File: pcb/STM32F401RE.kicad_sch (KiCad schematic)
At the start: 0 parts

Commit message: Connected oscillator to controller. Fixed local/hierarchical labeling in sheet.
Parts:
- added C5, C6: 22 pF, symbol Device:C
- added U3: STM32F401RETx, Package_QFP:LQFP-64_10x10mm_P0.5mm, symbol MCU_ST_STM32F4:STM32F401RETx
- added Y2: CX3225SB16000H0FLJCC, CX3225SB16000H0FLJCC:OSCCC320X250X60N, symbol 16 MHz Oscillator:CX3225SB16000H0FLJCC
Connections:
- new net: U3.18 (VSS), U3.31 (VSS), U3.47 (VSS), U3.63 (VSS)
- new net GND: Y2.2 (GND), Y2.4 (GND)

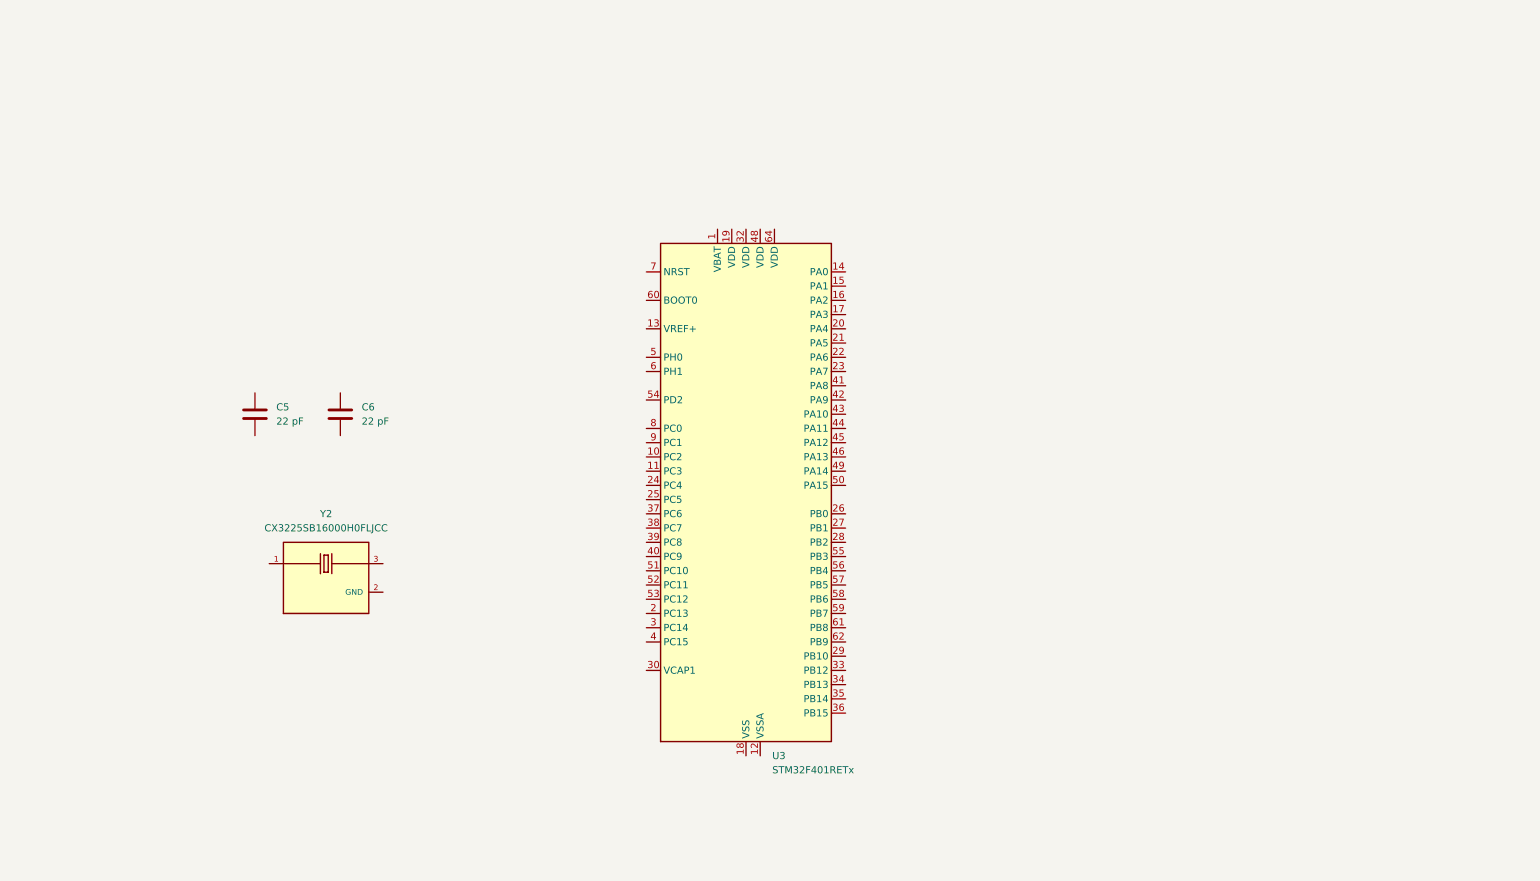
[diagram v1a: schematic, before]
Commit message: Added Front and Rear zone sheets made of CAN and MCU design sheets.
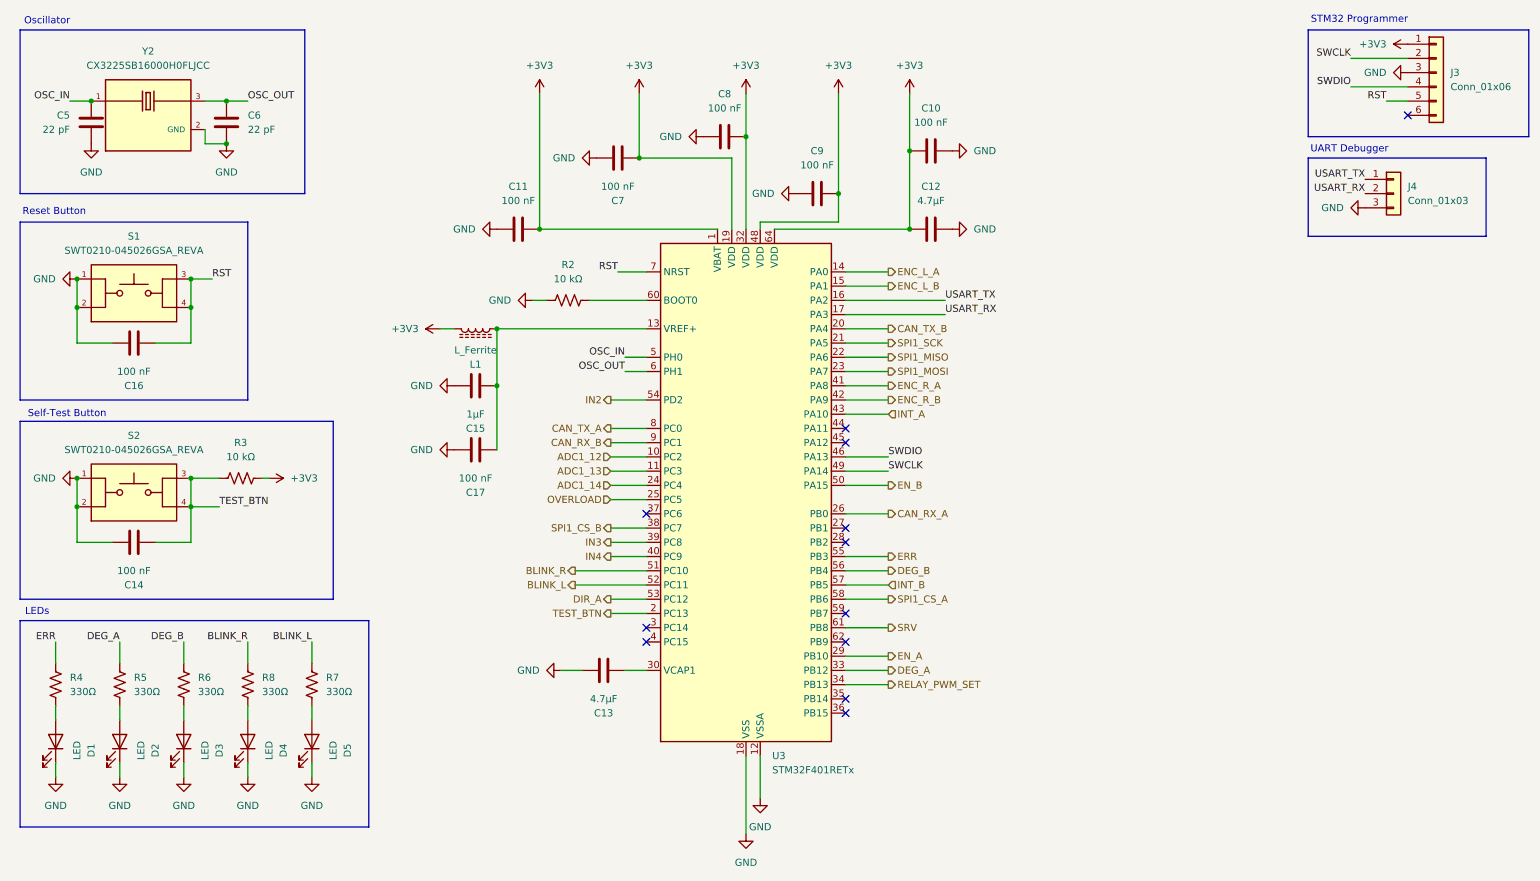
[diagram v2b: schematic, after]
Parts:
- added C10, C11, C14, C16, C17, C7, C8, C9: 100 nF, symbol Device:C
- added C12, C13: 4.7μF, symbol Device:C
- added C15: 1μF, symbol Device:C
- added D1, D2, D3, D4, D5: LED, symbol Device:LED
- added J3: Conn_01x06, symbol Connector_Generic:Conn_01x06
- added J4: Conn_01x03, symbol Connector_Generic:Conn_01x03
- added L1: L_Ferrite, symbol Device:L_Ferrite
- added R2, R3: 10 kΩ, symbol Device:R_US
- added R4, R5, R6, R7, R8: 330Ω, symbol Device:R_US
- added S1, S2: SWT0210-045026GSA_REVA, SWT0210-045026GSA_REVA:SW_SWT0210-045026GSA_REVA, symbol Push Button:SWT0210-045026GSA_REVA
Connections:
- net GND: now also C5.2, C6.2, U3.12 (VSSA), U3.18 (VSS), U3.31 (VSS), U3.47 (VSS), U3.63 (VSS), C10.1, C11.1, C12.2, C13.1, C14.1, C15.2, C16.1, C17.1, C7.1, C8.2, C9.1, D1.1 (K), D2.1 (K), D3.1 (K), D4.1 (K), D5.1 (K), J3.3 (Pin_3), J4.3 (Pin_3), R2.1, S1.1, S1.2, S2.1, S2.2
- net OSC_IN: now reaches C5.1
- net OSC_IN: now also U3.5 (PH0), Y2.1
- net +3V3: now reaches U3.1 (VBAT)
- net +3V3: now also U3.19 (VDD), U3.32 (VDD), U3.48 (VDD), U3.64 (VDD), C10.2, C11.2, C12.1, C7.2, C8.1, C9.2, J3.1 (Pin_1), L1.1, R3.2
- net ADC1_12: now reaches U3.10 (PC2)
- net ADC1_13: now reaches U3.11 (PC3)
- net at U3.13 (VREF+): now also C15.1, C17.2, L1.2
- net ENC_L_A: now reaches U3.14 (PA0)
- net ENC_L_B: now reaches U3.15 (PA1)
- net USART_TX: now reaches U3.16 (PA2)
- net USART_TX: now also J4.1 (Pin_1)
- net USART_RX: now reaches U3.17 (PA3)
- net USART_RX: now also J4.2 (Pin_2)
- net TEST_BTN: now reaches U3.2 (PC13)
- net TEST_BTN: now also C14.2, R3.1, S2.3, S2.4
- net CAN_TX_B: now reaches U3.20 (PA4)
- net SPI1_SCK: now reaches U3.21 (PA5)
- net SPI1_MISO: now reaches U3.22 (PA6)
- net SPI1_MOSI: now reaches U3.23 (PA7)
- net ADC1_14: now reaches U3.24 (PC4)
- net OVERLOAD: now reaches U3.25 (PC5)
- net CAN_RX_A: now reaches U3.26 (PB0)
- net EN_A: now reaches U3.29 (PB10)
- net at U3.30 (VCAP1): now also C13.2
- net DEG_A: now reaches U3.33 (PB12)
- net DEG_A: now also R5.1
- net RELAY_PWM_SET: now reaches U3.34 (PB13)
- net SPI1_CS_B: now reaches U3.38 (PC7)
- net IN3: now reaches U3.39 (PC8)
- net IN4: now reaches U3.40 (PC9)
- net ENC_R_A: now reaches U3.41 (PA8)
- net ENC_R_B: now reaches U3.42 (PA9)
- net INT_A: now reaches U3.43 (PA10)
- net SWDIO: now reaches U3.46 (PA13)
- net SWDIO: now also J3.4 (Pin_4)
- net SWCLK: now reaches U3.49 (PA14)
- net SWCLK: now also J3.2 (Pin_2)
- net EN_B: now reaches U3.50 (PA15)
- net BLINK_R: now reaches U3.51 (PC10)
- net BLINK_R: now also R8.1
- net BLINK_L: now reaches U3.52 (PC11)
- net BLINK_L: now also R7.1
- net DIR_A: now reaches U3.53 (PC12)
- net IN2: now reaches U3.54 (PD2)
- net ERR: now reaches U3.55 (PB3)
- net ERR: now also R4.1
- net DEG_B: now reaches U3.56 (PB4)
- net DEG_B: now also R6.1
- net INT_B: now reaches U3.57 (PB5)
- net SPI1_CS_A: now reaches U3.58 (PB6)
- net OSC_OUT: now reaches U3.6 (PH1)
- net OSC_OUT: now also C6.1, Y2.3
- net at U3.60 (BOOT0): now also R2.2
- net SRV: now reaches U3.61 (PB8)
- net RST: now reaches U3.7 (NRST)
- net RST: now also C16.2, J3.5 (Pin_5), S1.3, S1.4
- net CAN_TX_A: now reaches U3.8 (PC0)
- net CAN_RX_B: now reaches U3.9 (PC1)
- new net: D2.2 (A), R5.2
- new net: D4.2 (A), R8.2
- new net: D5.2 (A), R7.2
- new net: D1.2 (A), R4.2
- new net: D3.2 (A), R6.2
- no-connect marks 0 -> 12
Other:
- note added: "LEDs"
- note added: "Oscillator"
- note added: "Reset Button"
- note added: "STM32 Programmer"
- note added: "Self-Test Button"
- note added: "UART Debugger"
- moved on the sheet: C5, C6, Y2

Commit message: Added footprints to all components.
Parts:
- C701: renamed from C5; value 22 pF -> 22pF; footprint (none) -> Capacitor_SMD:C_0603_1608Metric
- C702: renamed from C16; value 100 nF -> 100nF; footprint (none) -> Capacitor_SMD:C_0603_1608Metric
- C703: renamed from C14; value 100 nF -> 100nF; footprint (none) -> Capacitor_SMD:C_0603_1608Metric
- C704: renamed from C6; value 22 pF -> 22pF; footprint (none) -> Capacitor_SMD:C_0603_1608Metric
- C705: renamed from C15; footprint (none) -> Capacitor_SMD:C_0603_1608Metric
- C706: renamed from C17; value 100 nF -> 100nF; footprint (none) -> Capacitor_SMD:C_0603_1608Metric
- C707: renamed from C11; value 100 nF -> 100nF; footprint (none) -> Capacitor_SMD:C_0603_1608Metric
- C708: renamed from C13; footprint (none) -> Capacitor_SMD:C_0805_2012Metric
- C709: renamed from C7; value 100 nF -> 100nF; footprint (none) -> Capacitor_SMD:C_0603_1608Metric
- C710: renamed from C8; value 100 nF -> 100nF; footprint (none) -> Capacitor_SMD:C_0603_1608Metric
- C711: renamed from C9; value 100 nF -> 100nF; footprint (none) -> Capacitor_SMD:C_0603_1608Metric
- C712: renamed from C10; value 100 nF -> 100nF; footprint (none) -> Capacitor_SMD:C_0603_1608Metric
- C713: renamed from C12; footprint (none) -> Capacitor_SMD:C_0805_2012Metric
- D701: renamed from D1; footprint (none) -> LED_SMD:LED_0603_1608Metric
- D702: renamed from D2; footprint (none) -> LED_SMD:LED_0603_1608Metric
- D703: renamed from D3; footprint (none) -> LED_SMD:LED_0603_1608Metric
- D704: renamed from D4; footprint (none) -> LED_SMD:LED_0603_1608Metric
- D705: renamed from D5; footprint (none) -> LED_SMD:LED_0603_1608Metric
- J701: renamed from J4; footprint (none) -> Connector_PinHeader_2.54mm:PinHeader_1x03_P2.54mm_Vertical
- J702: renamed from J3; footprint (none) -> Connector_PinHeader_2.54mm:PinHeader_1x06_P2.54mm_Vertical
- L701: renamed from L1; footprint (none) -> Inductor_SMD:L_0603_1608Metric
- R701: renamed from R4; footprint (none) -> Resistor_SMD:R_0603_1608Metric
- R702: renamed from R5; footprint (none) -> Resistor_SMD:R_0603_1608Metric
- R703: renamed from R6; footprint (none) -> Resistor_SMD:R_0603_1608Metric
- R704: renamed from R3; value 10 kΩ -> 10kΩ; footprint (none) -> Resistor_SMD:R_0603_1608Metric
- R705: renamed from R8; footprint (none) -> Resistor_SMD:R_0603_1608Metric
- R706: renamed from R7; footprint (none) -> Resistor_SMD:R_0603_1608Metric
- R707: renamed from R2; value 10 kΩ -> 10kΩ; footprint (none) -> Resistor_SMD:R_0603_1608Metric
- renumbered S1 to S701, S2 to S702, U3 to U701, Y2 to Y701

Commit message: Added CAN Bus connectors and finalized schematic with BOM, LCSC #s, and links to parts.
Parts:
- C701, C704: LCSC (none) -> C2168649; MPN (none) -> C0603C220J1GACTU; Manufacturer (none) -> KEMET
- C702, C703, C706, C707, C709, C710, C711, C712: LCSC (none) -> C18522636; MPN (none) -> KGM15AR71C104KT; Manufacturer (none) -> KYOCERA AVX
- C705: LCSC (none) -> C519560; MPN (none) -> CC0603JRX7R7BB105; Manufacturer (none) -> YAGEO
- C708, C713: LCSC (none) -> C408144; MPN (none) -> GRM21BR71C475KE51L; Manufacturer (none) -> Murata
- D701, D702, D703: LCSC (none) -> C94869; MPN (none) -> LTST-C190KRKT; Manufacturer (none) -> Lite-On
- D704, D705: LCSC (none) -> C125095; MPN (none) -> LTST-C190KSKT; Manufacturer (none) -> Lite-On
- J701: LCSC (none) -> C2937625; MPN (none) -> PZ254V-11-03P
- J702: LCSC (none) -> C492405; MPN (none) -> PZ254V-11-06P
- L701: LCSC (none) -> C2650942; MPN (none) -> 742863160; Manufacturer (none) -> Würth Elektronik
- R701, R702, R703, R705, R706: LCSC (none) -> C105881; MPN (none) -> RC0603FR-07330RL; Manufacturer (none) -> YAGEO
- R704, R707: LCSC (none) -> C844918; MPN (none) -> CRCW060310K0FKEA; Manufacturer (none) -> Vishay Dale
- S701, S702: LCSC (none) -> N/A - shelf part; MPN (none) -> SWT0210-045026GSA; Manufacturer (none) -> GCT
- U701: LCSC (none) -> C2053837; MPN (none) -> STM32F401RET6TR; Manufacturer (none) -> STMicroelectronics
- Y701: LCSC (none) -> C1985207; MPN (none) -> CX3225SB16000H0FLJCC; Manufacturer (none) -> KYOCERA AVX
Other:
- company: (none) -> 18-649 Lab 4: Controller PCB
- title: (none) -> Zone MCU: STM32F401RET6 (Front and Rear)
